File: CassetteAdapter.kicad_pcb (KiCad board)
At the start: 2 copper layers, 41 x 42.5 mm, 17 parts, among them CN1 AUDIO_IN, CN2 TAPE_PORT, U1 CD4049, U2 LM741

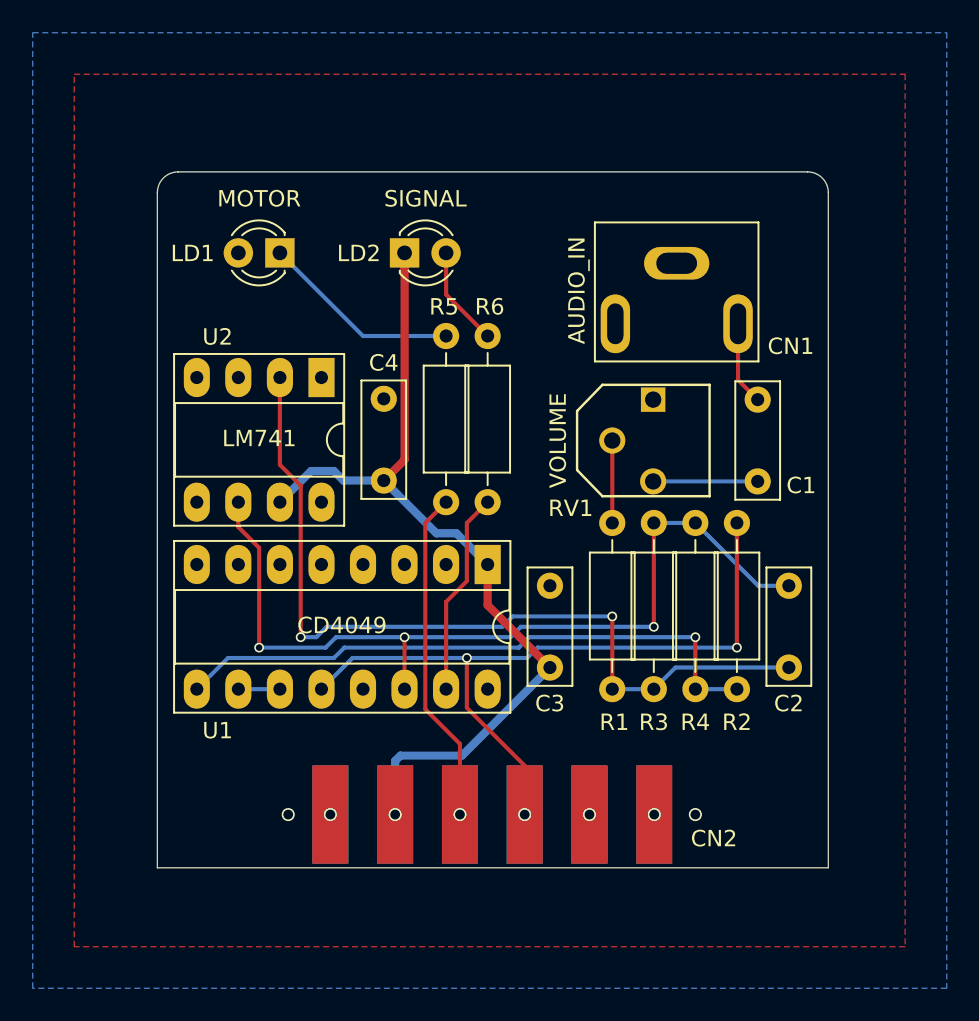
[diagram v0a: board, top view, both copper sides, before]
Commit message: Add 3.5" jack and ready for V1
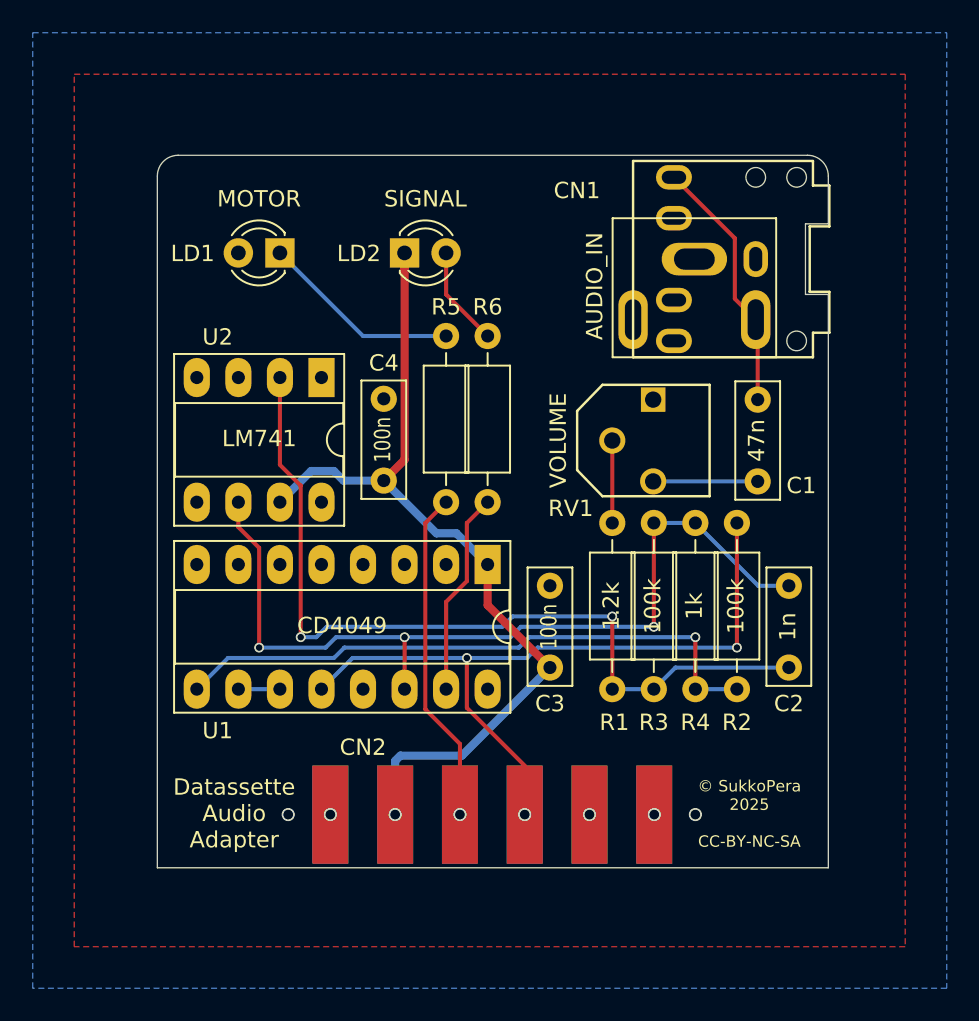
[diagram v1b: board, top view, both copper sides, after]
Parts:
- added CN101: AUDIO_IN_JACK, CassetteAdapter:AudioJack_SJ1-3525N, F.Cu at (148.3, 72.3)
- added V0: OSHW_LOGO, CassetteAdapter:cc_by_nc_sa_small, B.Cu at (132.3, 83.4)
- moved CN1 1.11 mm to (144.6, 72.3)
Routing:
- net Net-(C1-Pad2): track 5.13 -> 15.7 mm
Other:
- board size 41 x 42.5 mm -> 41 x 43.6 mm
- board text added: "Datassette Audio Adapter"
- board text added: "V1"
- board text added: "github.com/SukkoPera/ DatassetteAudioAdapter"
- board text added: "© SukkoPera 2025 CC-BY-NC-SA"

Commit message: Fix volume pot, volume should now increase clockwise
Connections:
- RV1 pad 1: GND -> Net-(C1-Pad1)
- RV1 pad 3: Net-(C1-Pad1) -> GND
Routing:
- net Net-(C1-Pad1): track 6.39 -> 8.46 mm
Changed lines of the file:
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@@
     (thickness 1.6)
     (drawings 18)
-    (tracks 97)
+    (tracks 98)
     (zones 0)
     (modules 19)
@@
     (fp_line (start 3.405 -1.85) (end 1.805 -3.4) (layer F.SilkS) (width 0.15))
     (pad 1 thru_hole rect (at 2.5 1.25 90) (size 1.5 1.5) (drill 1) (layers *.Cu *.Mask)
-      (net 6 GND))
+      (net 1 "Net-(C1-Pad1)"))
     (pad 3 thru_hole circle (at -2.5 1.25 90) (size 1.6 1.6) (drill 1) (layers *.Cu *.Mask)
-      (net 1 "Net-(C1-Pad1)"))
+      (net 6 GND))
     (pad 2 thru_hole circle (at 0 -1.25 90) (size 1.6 1.6) (drill 1) (layers *.Cu *.Mask)
       (net 11 "Net-(R1-Pad2)"))
@@
   (gr_line (start 111.76 109.474) (end 152.781 109.474) (layer Edge.Cuts) (width 0.05))
   (gr_line (start 111.76 67.183) (end 111.76 109.474) (layer Edge.Cuts) (width 0.05))
-  (segment (start 142.073 85.852) (end 148.463 85.852) (width 0.25) (layer B.Cu) (net 1))
+  (segment (start 147.073 85.852) (end 142.073 80.852) (width 0.25) (layer B.Cu) (net 1))
+  (segment (start 148.463 85.852) (end 147.073 85.852) (width 0.25) (layer B.Cu) (net 1))
   (segment (start 148.463 76.082) (end 148.343 75.962) (width 0.25) (layer F.Cu) (net 2))
   (segment (start 148.463 80.852) (end 148.463 76.082) (width 0.25) (layer F.Cu) (net 2))

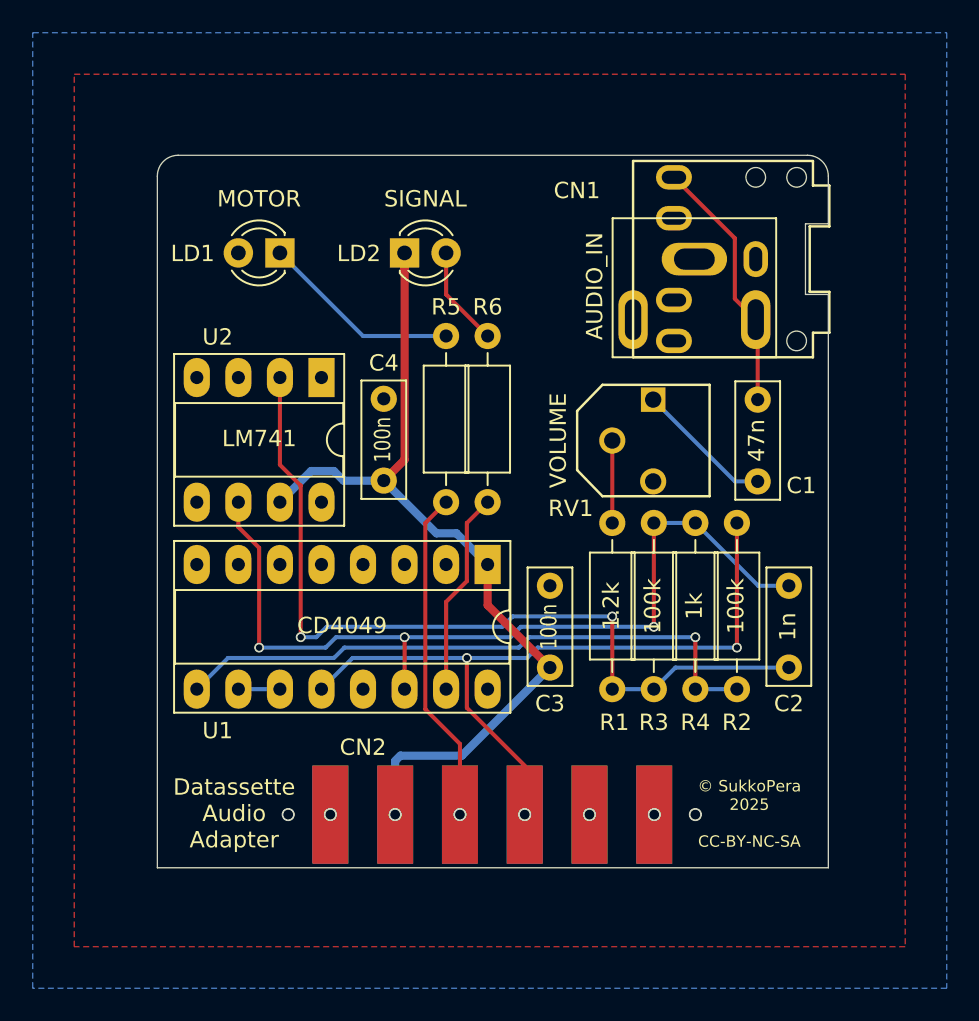
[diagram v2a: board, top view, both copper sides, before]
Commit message: Add possibility to invert signal
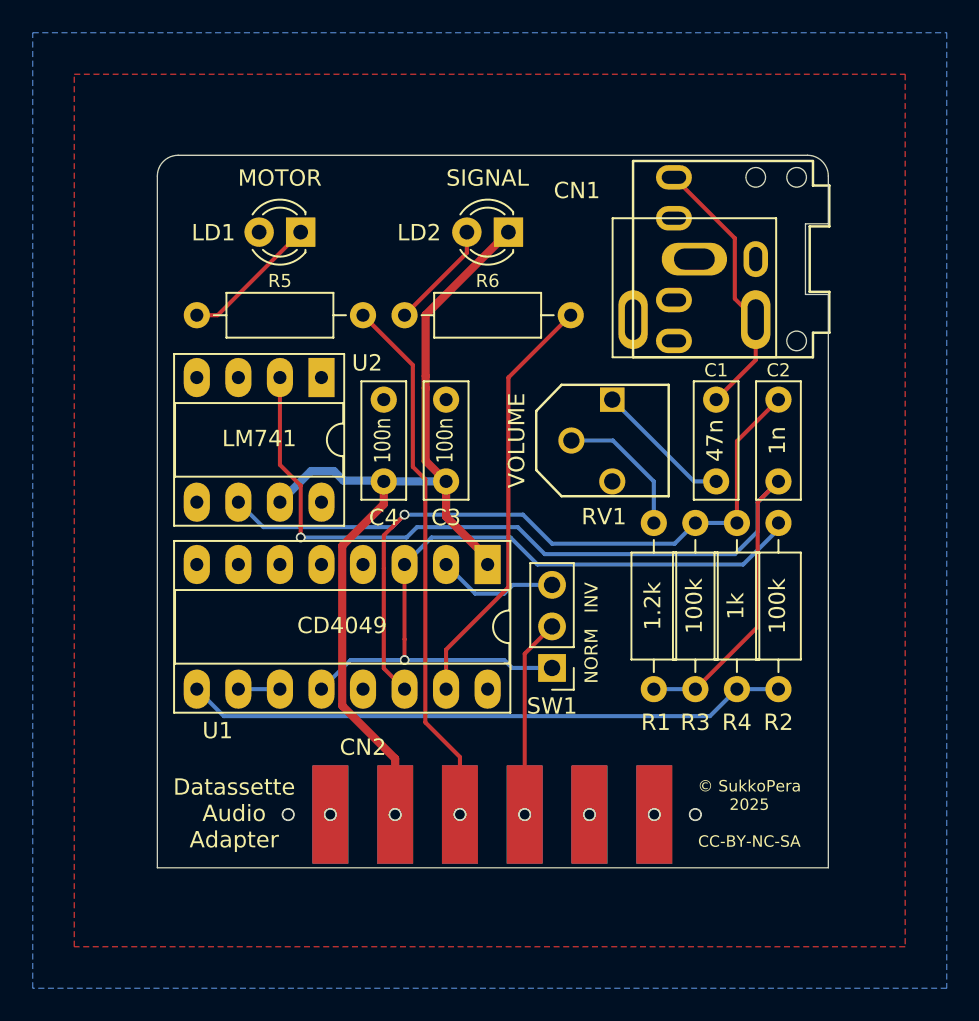
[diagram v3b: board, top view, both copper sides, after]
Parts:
- added SW1: SW_INVERT1, Connector_PinHeader_2.54mm:PinHeader_1x03_P2.54mm_Vertical, F.Cu at (135.9, 97.3)
- moved V0 16.9 mm to (144.8, 94.7)
- moved C3 13.0 mm to (129.4, 80.9)
- moved R5 12.5 mm to (124.3, 75.7), turned to 180 degrees
- moved C2 11.4 mm to (149.7, 80.9)
- moved LD2 6.48 mm to (133.2, 70.6), turned to 180 degrees
- moved R6 5.24 mm to (126.9, 75.7), turned to 0 degrees
- moved R4 2.54 mm to (147.2, 98.6)
- moved C1 2.54 mm to (145.9, 85.9)
- moved R1 2.54 mm to (142.1, 98.6)
- moved R2 2.54 mm to (149.7, 98.6)
- moved R3 2.54 mm to (144.7, 88.4)
- moved RV1 2.50 mm to (138.3, 83.4)
- moved LD1 1.80 mm to (120.5, 70.6)
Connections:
- R2 pad 2: /read -> Net-(R2-Pad2)
- U1 pad 12: /read -> Net-(R2-Pad2)
- U1 pad 3: GND -> Net-(R2-Pad2)
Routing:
- net Net-(R2-Pad2): track 0.00 -> 46.4 mm, vias 0 -> 1
- net /read: track 45.1 -> 12.2 mm, vias 3 -> 1
- net Net-(R6-Pad2): track 12.5 -> 26.0 mm
- net /motor: track 20.5 -> 33.0 mm
- net Net-(C2-Pad2): track 51.8 -> 60.7 mm, vias 2 -> 1
- net Net-(SW1-Pad3): track 0.00 -> 7.43 mm
- net +5V: track 53.7 -> 57.9 mm
- net Net-(LD1-Pad1): track 12.3 -> 8.45 mm
- net Net-(R1-Pad2): track 5.04 -> 8.62 mm
- net Net-(C1-Pad2): track 15.7 -> 16.7 mm
- net Net-(R2-Pad1): track 37.5 -> 36.9 mm, vias 1 -> 0
- net Net-(LD2-Pad2): track 6.13 -> 6.66 mm
- net Net-(C2-Pad1): track 53.4 -> 53.0 mm, vias 3 -> 1
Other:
- board text added: "INV"
- board text added: "NORM"

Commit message: Fix LEDs
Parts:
- moved LD2 2.54 mm to (130.7, 70.6), turned to 0 degrees
- moved LD1 2.54 mm to (118.0, 70.6), turned to 0 degrees
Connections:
- LD1 pad 1: Net-(LD1-Pad1) -> GND
- LD1 pad 2: GND -> Net-(LD1-Pad2)
- LD2 pad 1: +5V -> Net-(LD2-Pad1)
- LD2 pad 2: Net-(LD2-Pad2) -> +5V
- R5 pad 2: Net-(LD1-Pad1) -> Net-(LD1-Pad2)
- R6 pad 1: Net-(LD2-Pad2) -> Net-(LD2-Pad1)
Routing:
- net Net-(LD1-Pad2): track 0.00 -> 8.45 mm
- net Net-(LD1-Pad1): track 8.45 -> 0.00 mm
- net Net-(LD2-Pad2): track 6.66 -> 0.00 mm
- net Net-(LD2-Pad1): track 0.00 -> 6.66 mm

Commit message: Fix edge connector orientation, sigh...
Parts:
- moved R6 10.2 mm to (137.0, 75.7), turned to 180 degrees
- moved LD2 2.54 mm to (133.2, 70.6), turned to 180 degrees
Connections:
- CN2 pad 2: /write -> +5V
- CN2 pad 3: /read -> /motor
- CN2 pad 4: /motor -> /read
- CN2 pad 5: +5V -> /write
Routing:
- net /read: track 12.2 -> 24.3 mm, vias 1 -> 2
- net +5V: track 57.9 -> 52.0 mm
- net /motor: track 33.0 -> 36.5 mm
- net Net-(R6-Pad2): track 26.0 -> 25.0 mm
- net Net-(R2-Pad1): track 36.9 -> 37.7 mm

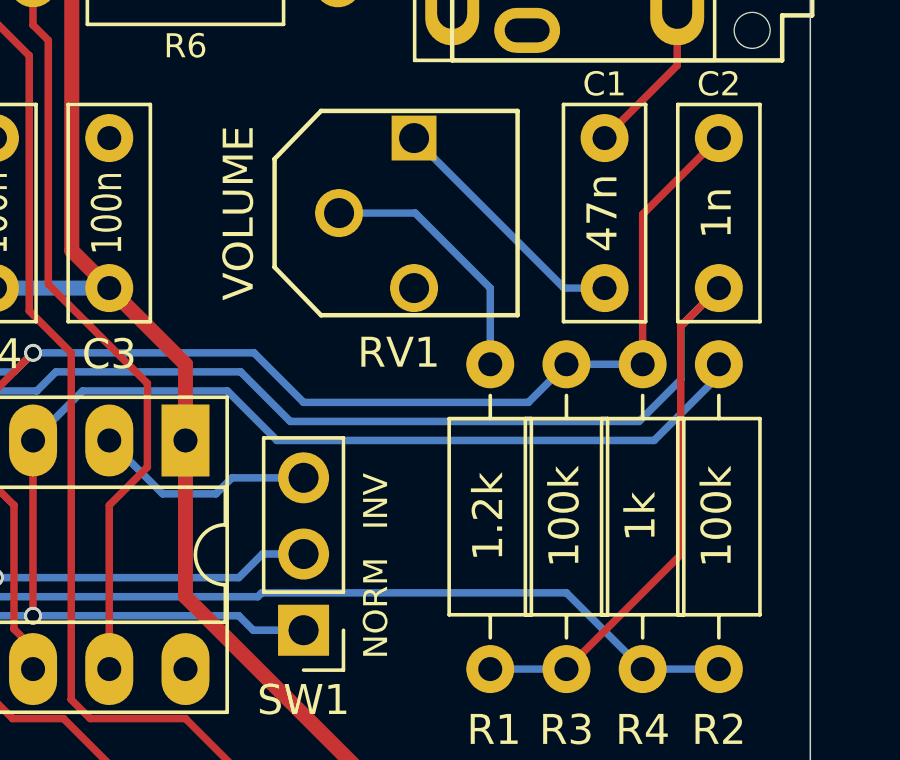
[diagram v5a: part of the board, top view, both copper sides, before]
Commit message: More common component values
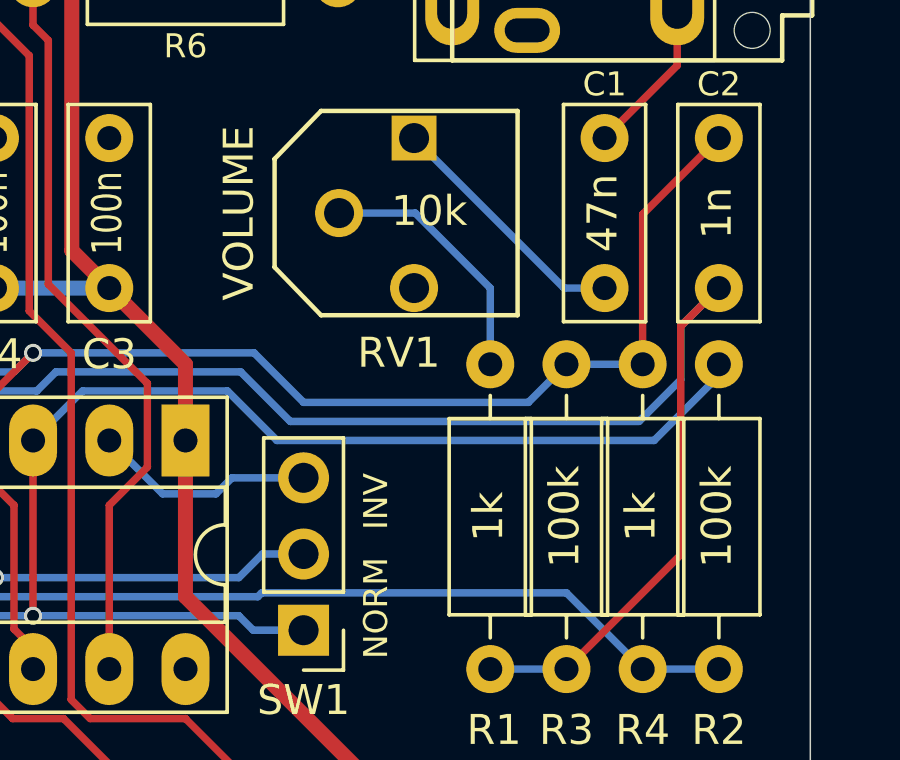
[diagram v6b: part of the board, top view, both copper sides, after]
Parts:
- R1: value 1.2k -> 1k
- RV1: value 15k -> 10k
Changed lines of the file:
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@@
       (effects (font (size 1 1) (thickness 0.15)))
     )
-    (fp_text value 15k (at 0 5.8 90) (layer F.Fab)
+    (fp_text value 10k (at 0.0675 1.758 180) (layer F.SilkS)
       (effects (font (size 1 1) (thickness 0.15)))
     )
@@
       (effects (font (size 1 1) (thickness 0.15)))
     )
-    (fp_text value 1.2k (at 5.08 -0.0675 90) (layer F.SilkS)
+    (fp_text value 1k (at 5.08 -0.0675 90) (layer F.SilkS)
       (effects (font (size 1 1) (thickness 0.15)))
     )

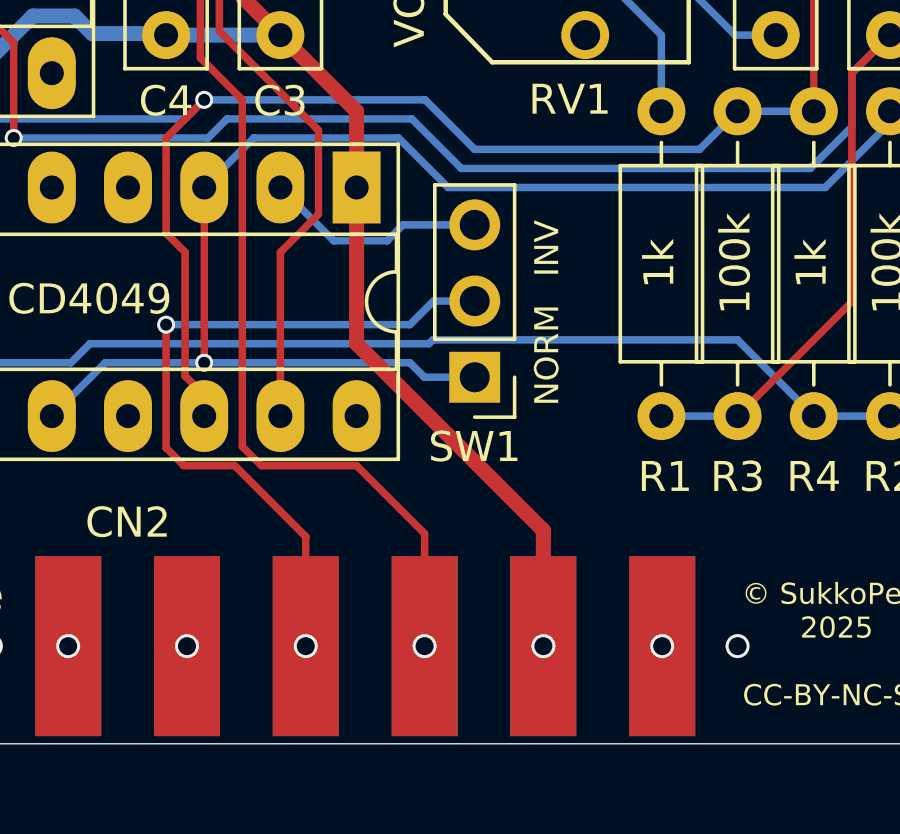
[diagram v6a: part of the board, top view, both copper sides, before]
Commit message: LED resistors -> 1k
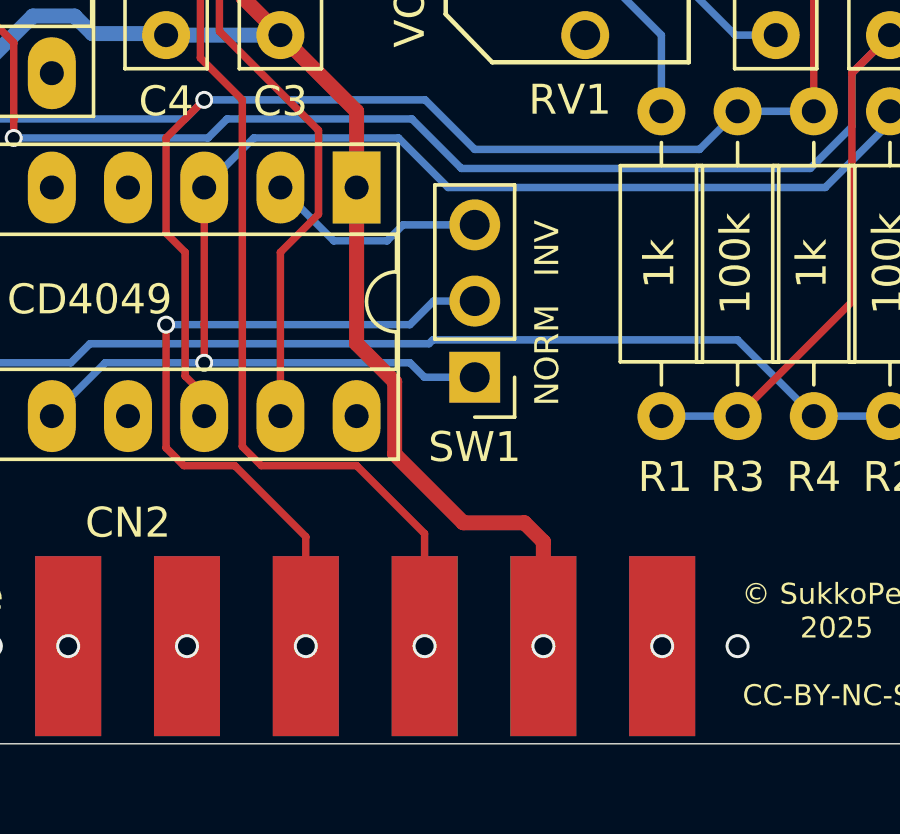
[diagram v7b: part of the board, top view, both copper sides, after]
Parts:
- R5, R6: value 1.2k -> 1k
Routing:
- net +5V: track 52.0 -> 53.2 mm
